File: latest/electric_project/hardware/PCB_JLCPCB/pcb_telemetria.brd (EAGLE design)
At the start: 106.8 x 121.5 mm, 39 parts

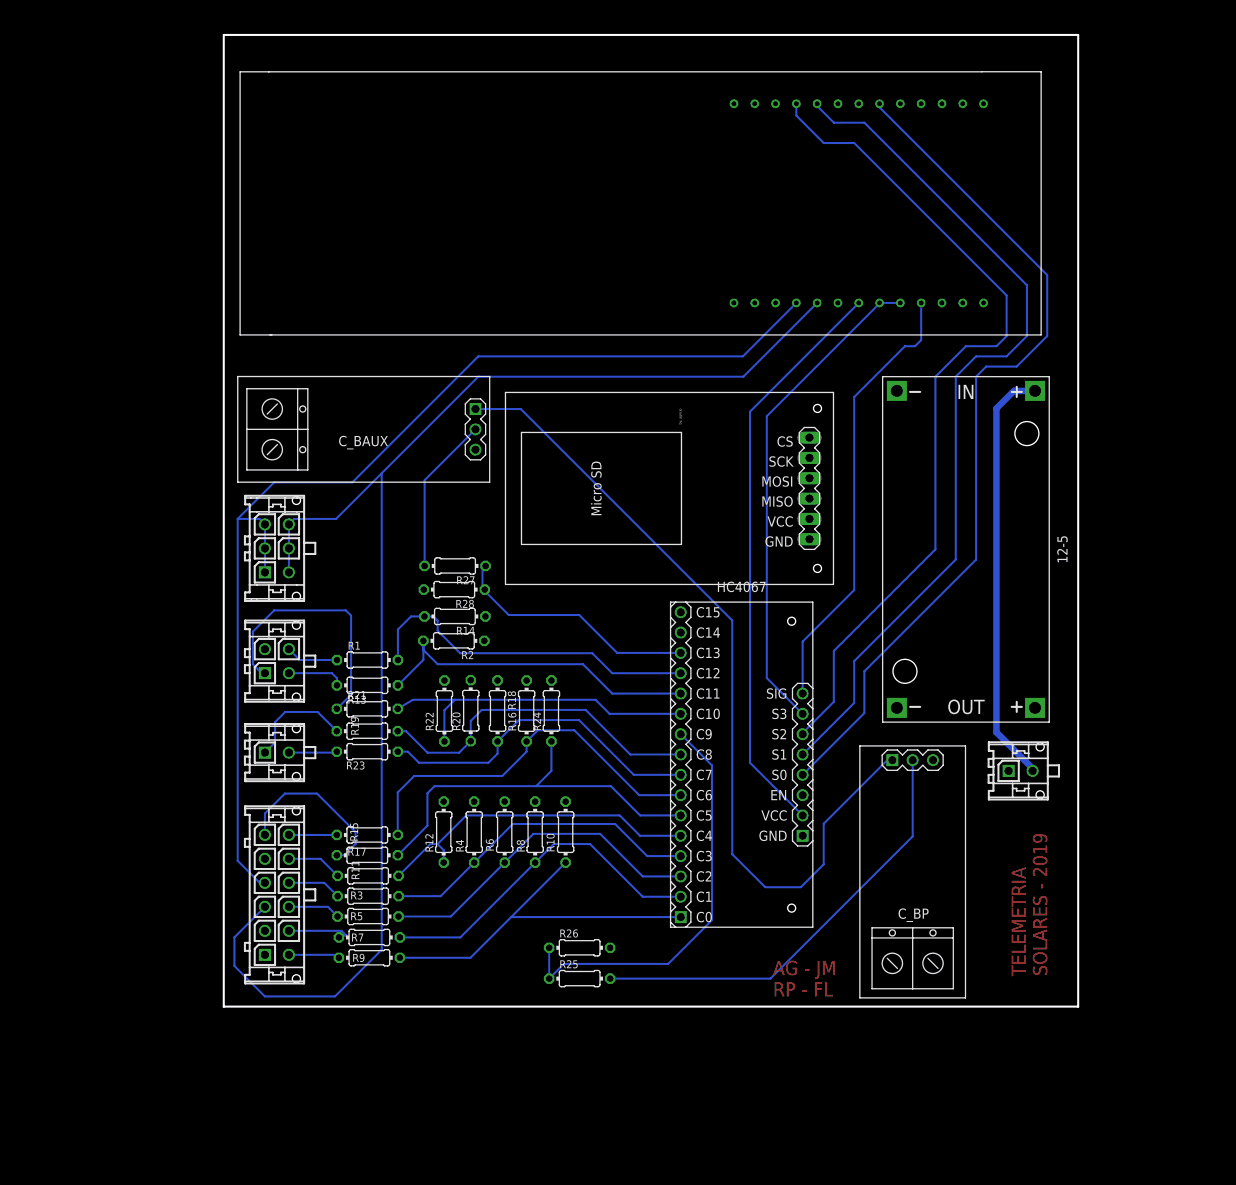
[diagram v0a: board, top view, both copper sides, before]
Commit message: adicao de conexao para pinos extras
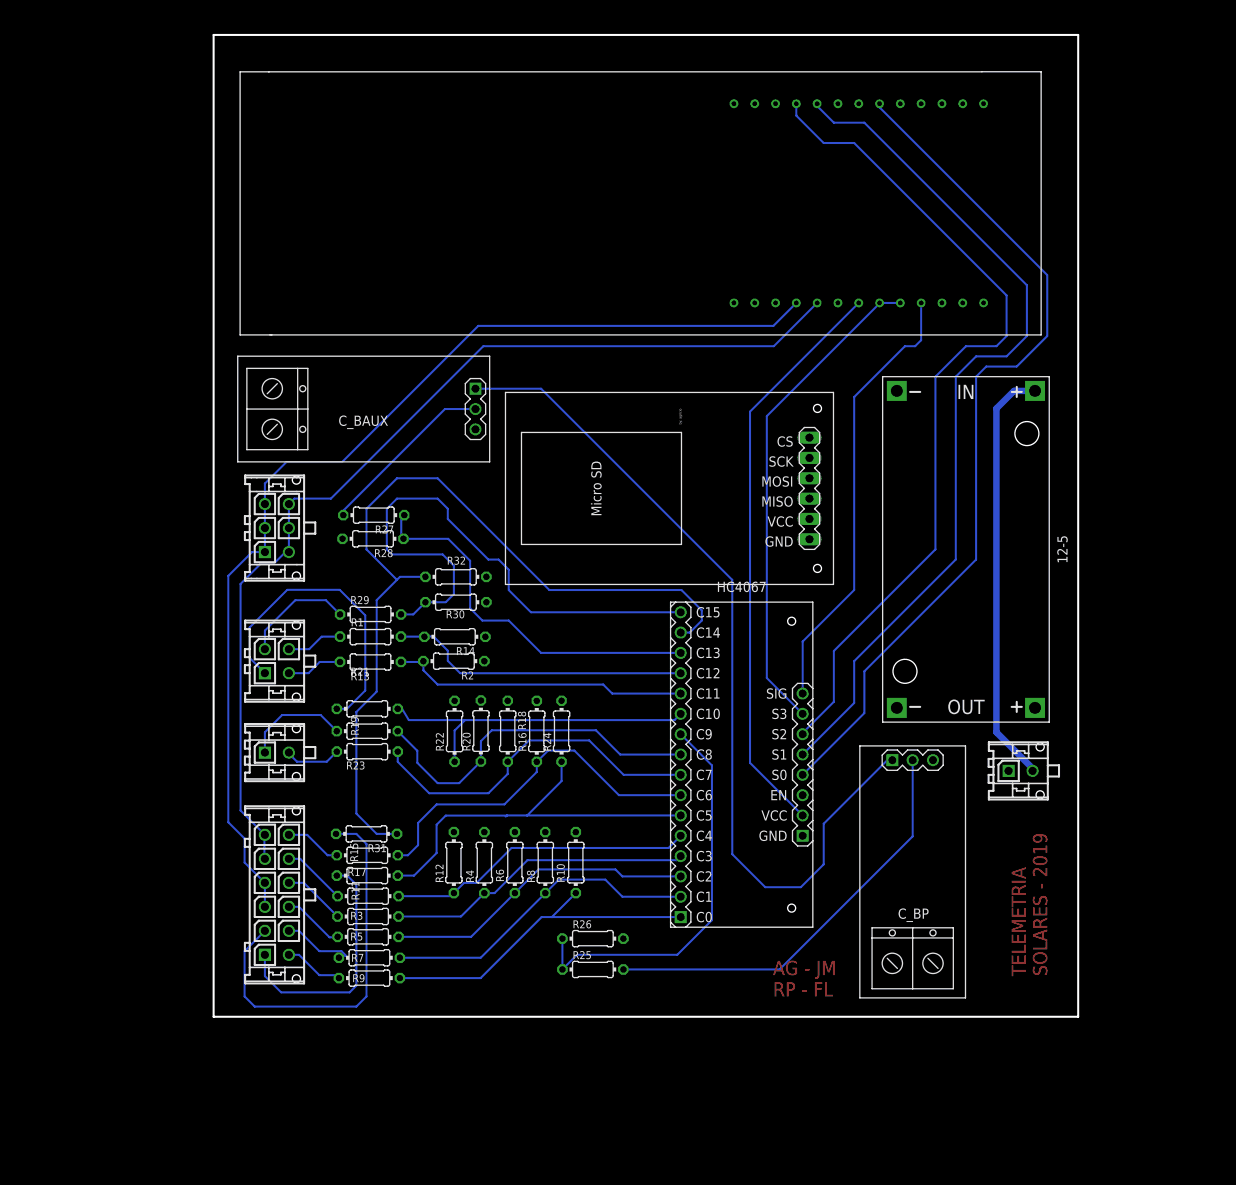
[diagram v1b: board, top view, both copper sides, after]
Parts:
- added R29, R31: 2.2k, rcl:0204/7
- added R30, R32: 3.9k, rcl:0204/7
- moved R27 12.0 mm to (22.5, 56.4)
- moved R28 12.0 mm to (22.4, 53.4)
- moved R10 4.02 mm to (47.8, 12.9)
- moved R4 4.02 mm to (36.3, 12.9)
- moved R8 4.02 mm to (43.9, 12.9)
- moved R12 4.02 mm to (32.5, 12.9)
- moved R6 4.02 mm to (40.1, 12.9)
- moved R1 2.95 mm to (22.1, 41.2)
- moved R13 2.95 mm to (22.1, 38.0)
- moved R22 2.84 mm to (32.6, 29.3)
- moved R16 2.84 mm to (42.9, 29.3)
- moved R18 2.84 mm to (39.2, 29.3)
- moved R20 2.84 mm to (35.9, 29.4)
- moved R24 2.84 mm to (46.0, 29.3)
- moved R11 2.54 mm to (21.8, 8.72)
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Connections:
- removed net N$5: X1.P$2
- removed net N$6: X1.P$1
- removed net N$8: X1.P$5
- new net EXTRA1: R29.1, X3.P$2
- new net EXTRA2: R31.2, X1.P$2
- net 21: now also X1.P$3
- net 22: now also X1.P$5, X1.P$6; no longer X1.P$3
- net BE_IN: now also X1.P$1; no longer X1.P$6
- net C14: now also R31.1, R32.2
- net C15: now also R29.2, R30.1
- net GND: now also R30.2, R32.1
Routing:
- net C14: track 0.00 -> 106.5 mm
- net C15: track 0.00 -> 70.9 mm
- net EXTRA2: track 0.00 -> 48.9 mm
- net 22: track 174.4 -> 126.0 mm
- net C13: track 31.1 -> 47.3 mm
- net EXTRA1: track 0.00 -> 14.0 mm
- net BE_IN: track 21.4 -> 30.8 mm
- net BAT_AUX: track 32.1 -> 38.1 mm
- net C12: track 43.5 -> 37.6 mm
- net C11: track 42.4 -> 37.4 mm
- net 21: track 138.0 -> 133.4 mm
- net C0: track 46.8 -> 42.5 mm
- net VCC: track 103.5 -> 107.6 mm
- net C4: track 42.1 -> 38.4 mm
- net C1: track 42.7 -> 40.0 mm
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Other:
- board size 106.8 x 121.5 mm -> 108.1 x 122.7 mm

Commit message: adding connector to sd card and capacitors
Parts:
- added C1, C2: 0.1uF, rcl:E5-5
- added C3: (no value), rcl:E5-5
- added X6: (no value), con-molex-micro-fit-3_0:43045-0412
- moved U$2 117.0 mm to (-10.2, -18.4), turned to 0 degrees
- moved X4 3.72 mm to (102.4, 20.7)
- moved C_BP 1.42 mm to (91.1, 12.4)
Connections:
- new net N$3: U$2.3, X6.P$4
- new net N$4: U$2.4, X6.P$3
- new net N$6: U$2.6, X6.P$1
- new net N$7: U$2.5, X6.P$2
- net GND: now also C1.-, C2.-, C3.-
- net VCC: now also C1.+, C3.+
- net VI: now also C2.+
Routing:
- net VCC: track 107.6 -> 143.0 mm
- net VI: track 52.9 -> 63.7 mm
- net N$1: track 52.6 -> 57.1 mm
- net 4: track 55.7 -> 55.0 mm

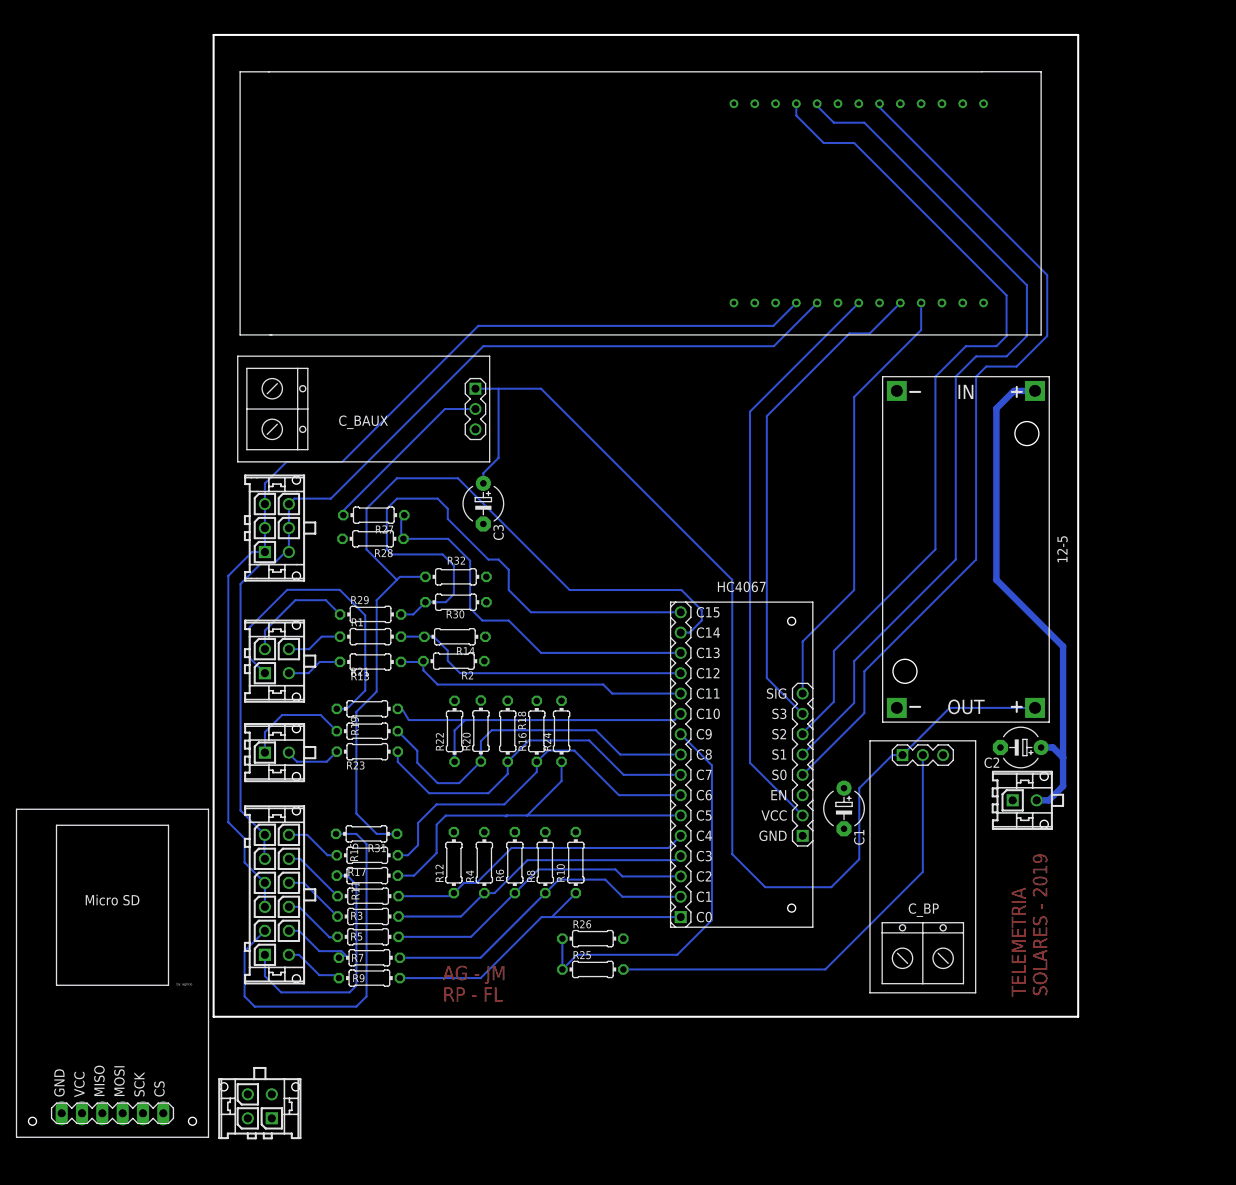
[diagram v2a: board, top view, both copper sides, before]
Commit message: adding connector to sdcard and ground plane
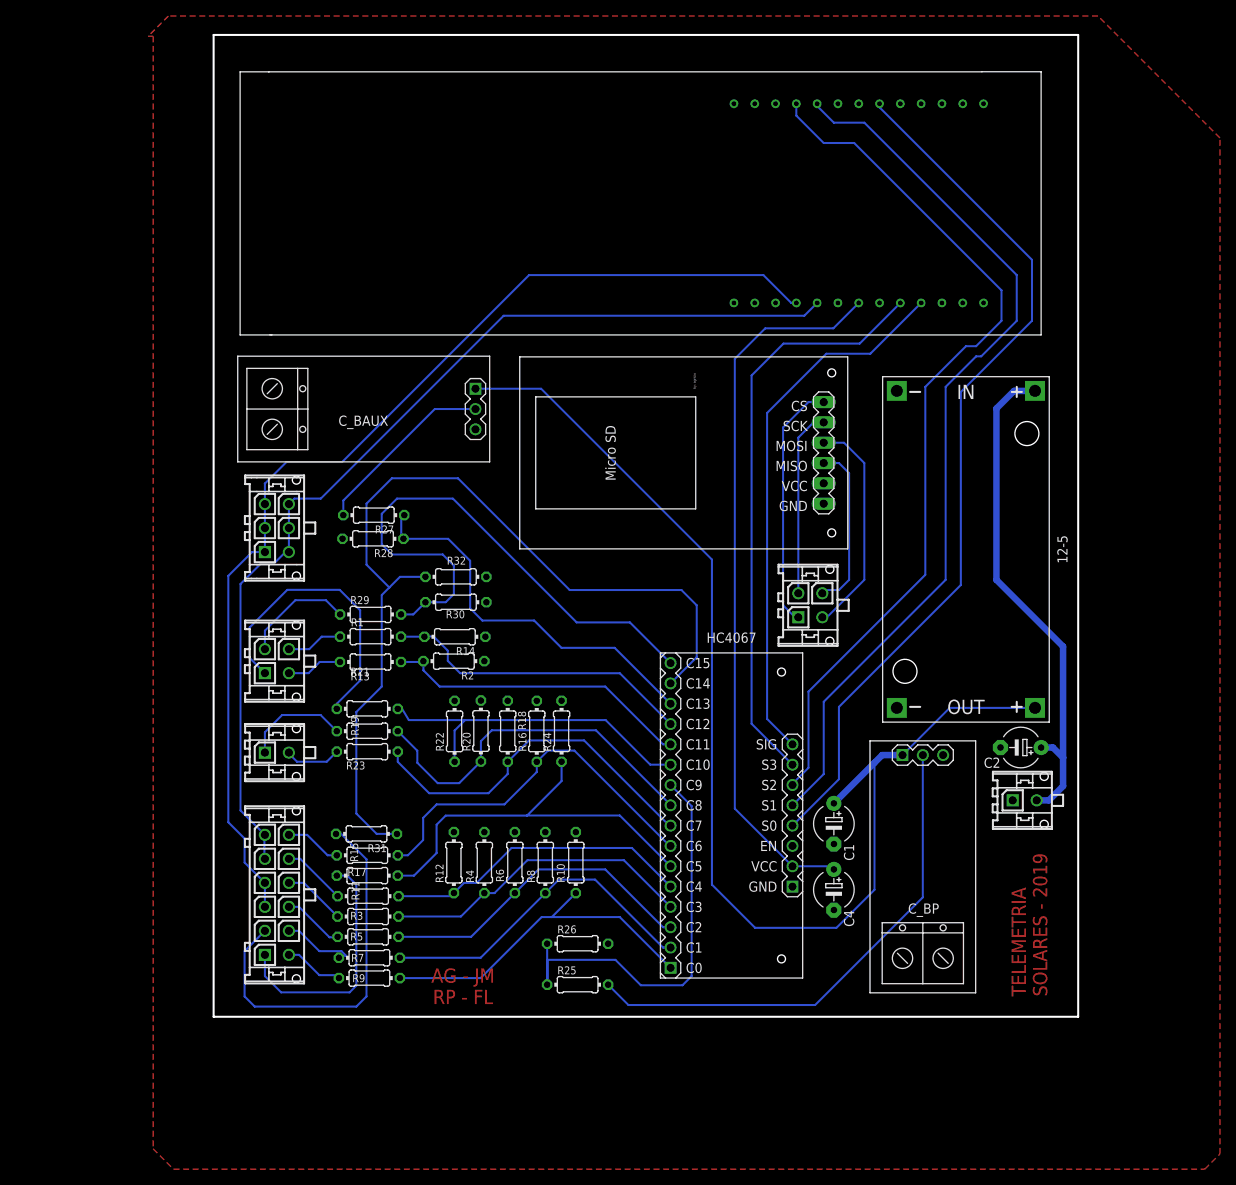
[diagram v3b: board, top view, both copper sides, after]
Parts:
- removed C3: (no value), rcl:E5-5
- added C4: (no value), rcl:E5-5
- moved U$2 121.3 mm to (78.7, 64.1), turned to 90 degrees
- moved X6 93.0 mm to (75.6, 45.1), turned to 270 degrees
- moved HC4067 6.48 mm to (67.2, 18.8)
- moved R25 2.69 mm to (48.0, -2.34)
- moved C1 2.29 mm to (80.0, 17.8)
- moved R26 2.01 mm to (48.0, 2.78)
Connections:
- net 3V3: now also C4.+
- net GND: now also C4.-; no longer C3.-
- net VCC: no longer C3.+
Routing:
- net N$6: track 0.00 -> 31.1 mm
- net N$4: track 0.00 -> 27.9 mm
- net N$7: track 0.00 -> 23.4 mm
- net N$3: track 0.00 -> 21.1 mm
- net 3V3: track 72.4 -> 90.1 mm
- net 4: track 55.0 -> 67.7 mm
- net 0: track 61.6 -> 73.1 mm
- net N$1: track 57.1 -> 63.7 mm
- net C14: track 106.5 -> 113.1 mm
- net VCC: track 143.0 -> 149.5 mm
- net 13: track 104.7 -> 109.6 mm
- net 14: track 108.3 -> 112.2 mm
- net 32: track 107.5 -> 110.5 mm
- net C9: track 50.0 -> 53.0 mm
- net 21: track 133.4 -> 136.3 mm
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- added copper zone on layer 1, net GND

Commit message: up
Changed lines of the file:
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@@
 <?xml version="1.0" encoding="utf-8"?>
 <!DOCTYPE eagle SYSTEM "eagle.dtd">
-<eagle version="9.5.0">
+<eagle version="9.5.1">
 <drawing>
 <settings>
@@
 <wire x1="74.83855625" y1="22.621246875" x2="74.83855625" y2="22.76855625" width="0.254" layer="16"/>
 <wire x1="74.83855625" y1="22.76855625" x2="76.835" y2="24.765" width="0.254" layer="16"/>
-<wire x1="76.835" y1="24.765" x2="76.835" y2="34.29" width="0.254" layer="16"/>
-<wire x1="91.44" y1="48.895" x2="91.44" y2="72.39" width="0.254" layer="16"/>
+<wire x1="76.835" y1="24.765" x2="76.835" y2="33.655" width="0.254" layer="16"/>
+<wire x1="91.44" y1="48.26" x2="91.44" y2="72.39" width="0.254" layer="16"/>
 <wire x1="91.44" y1="72.39" x2="96.52" y2="77.47" width="0.254" layer="16"/>
 <wire x1="97.79" y1="77.47" x2="100.965" y2="80.645" width="0.254" layer="16"/>
@@
 <wire x1="78.74" y1="102.87" x2="75.31951875" y2="106.29048125" width="0.254" layer="16"/>
 <wire x1="75.31951875" y1="106.29048125" x2="75.31951875" y2="107.777559375" width="0.254" layer="16"/>
-<wire x1="76.835" y1="34.29" x2="91.44" y2="48.895" width="0.254" layer="16"/>
+<wire x1="76.835" y1="33.655" x2="91.44" y2="48.26" width="0.254" layer="16"/>
 <wire x1="96.52" y1="77.47" x2="97.79" y2="77.47" width="0.254" layer="16"/>
 <wire x1="100.965" y1="84.455" x2="82.55" y2="102.87" width="0.254" layer="16"/>
@@
 <vertex x="-5.715" y="116.205"/>
 </polygon>
+<wire x1="80.51951875" y1="82.877559375" x2="70.11951875" y2="107.777559375" width="0" layer="19" extent="1-1"/>
+<wire x1="87.884" y1="71.882" x2="80.51951875" y2="82.877559375" width="0" layer="19" extent="1-1"/>
+<wire x1="87.884" y1="32.258" x2="87.884" y2="71.882" width="0" layer="19" extent="1-1"/>
+<wire x1="93.670121875" y1="26.360109375" x2="87.884" y2="32.258" width="0" layer="19" extent="1-1"/>
+<wire x1="100.838" y1="27.305" x2="93.670121875" y2="26.360109375" width="0" layer="19" extent="1-1"/>
+<wire x1="102.362" y1="20.701" x2="100.838" y2="27.305" width="0" layer="19" extent="1-1"/>
+<wire x1="80.01" y1="15.24" x2="93.670121875" y2="26.360109375" width="0" layer="19" extent="1-1"/>
+<wire x1="74.83855625" y1="15.001246875" x2="80.01" y2="15.24" width="0" layer="19" extent="1-1"/>
+<wire x1="74.83855625" y1="9.921246875" x2="74.83855625" y2="15.001246875" width="0" layer="19" extent="1-1"/>
+<wire x1="80.01" y1="6.985" x2="74.83855625" y2="9.921246875" width="0" layer="19" extent="1-1"/>
+<wire x1="51.7906" y1="2.778759375" x2="74.83855625" y2="9.921246875" width="0" layer="19" extent="1-1"/>
+<wire x1="47.752" y1="16.728446875" x2="51.7906" y2="2.778759375" width="0" layer="19" extent="1-1"/>
+<wire x1="43.942" y1="16.728446875" x2="47.752" y2="16.728446875" width="0" layer="19" extent="1-1"/>
+<wire x1="40.132" y1="16.728446875" x2="43.942" y2="16.728446875" width="0" layer="19" extent="1-1"/>
+<wire x1="36.322" y1="16.728446875" x2="40.132" y2="16.728446875" width="0" layer="19" extent="1-1"/>
+<wire x1="32.512" y1="16.728446875" x2="36.322" y2="16.728446875" width="0" layer="19" extent="1-1"/>
+<wire x1="32.5983625" y1="33.13684375" x2="32.512" y2="16.728446875" width="0" layer="19" extent="1-1"/>
+<wire x1="35.89020625" y1="33.177484375" x2="32.5983625" y2="33.13684375" width="0" layer="19" extent="1-1"/>
+<wire x1="39.243" y1="33.147" x2="35.89020625" y2="33.177484375" width="0" layer="19" extent="1-1"/>
+<wire x1="42.87520625" y1="33.13684375" x2="39.243" y2="33.147" width="0" layer="19" extent="1-1"/>
+<wire x1="36.322" y1="38.1" x2="35.89020625" y2="33.177484375" width="0" layer="19" extent="1-1"/>
+<wire x1="36.449" y1="41.148" x2="36.322" y2="38.1" width="0" layer="19" extent="1-1"/>
+<wire x1="36.576" y1="45.466" x2="36.449" y2="41.148" width="0" layer="19" extent="1-1"/>
+<wire x1="36.576" y1="48.641" x2="36.576" y2="45.466" width="0" layer="19" extent="1-1"/>
+<wire x1="35.209478125" y1="67.076315625" x2="36.576" y2="48.641" width="0" layer="19" extent="1-1"/>
+<wire x1="18.590259375" y1="53.393340625" x2="36.576" y2="48.641" width="0" layer="19" extent="1-1"/>
 </signal>
 <signal name="22">
 <contactref element="U$1" pad="22"/>
-<wire x1="15.875" y1="58.42" x2="38.735" y2="81.28" width="0.254" layer="16"/>
+<wire x1="17.145" y1="58.42" x2="40.005" y2="81.28" width="0.254" layer="16"/>
 <wire x1="76.321946875" y1="81.2799875" x2="77.91951875" y2="82.877559375" width="0.254" layer="16"/>
-<wire x1="76.321946875" y1="81.2799875" x2="38.735" y2="81.28" width="0.254" layer="16"/>
+<wire x1="76.321946875" y1="81.2799875" x2="40.005" y2="81.28" width="0.254" layer="16"/>
 <contactref element="X5" pad="P$5"/>
 <contactref element="X5" pad="P$6"/>
 <contactref element="X5" pad="P$4"/>
 <wire x1="11.89" y1="51.737" x2="11.89" y2="52.07" width="0.254" layer="16"/>
-<wire x1="11.89" y1="52.07" x2="11.89" y2="54.61" width="0.254" layer="16"/>
+<wire x1="11.89" y1="52.07" x2="11.89" y2="54.737" width="0.254" layer="16"/>
 <wire x1="11.89" y1="54.737" x2="11.89" y2="57.737" width="0.254" layer="16"/>
 <wire x1="11.89" y1="57.737" x2="12.573" y2="58.42" width="0.254" layer="16"/>
-<wire x1="12.573" y1="58.42" x2="15.875" y2="58.42" width="0.254" layer="16"/>
+<wire x1="12.573" y1="58.42" x2="17.145" y2="58.42" width="0.254" layer="16"/>
 <contactref element="X1" pad="P$6"/>
 <wire x1="8.89" y1="16.39" x2="8.83" y2="16.45" width="0.254" layer="16"/>
@@
 <wire x1="8.89" y1="13.39" x2="8.83" y2="13.45" width="0.254" layer="16"/>
 <wire x1="8.83" y1="13.45" x2="8.83" y2="16.45" width="0.254" layer="16"/>
-<wire x1="11.89" y1="54.737" x2="11.89" y2="54.61" width="0.254" layer="16"/>
 </signal>
 <signal name="21">
 <contactref element="U$1" pad="21"/>
-<wire x1="71.202103125" y1="86.359975" x2="41.91" y2="86.36" width="0.254" layer="16"/>
+<wire x1="71.202103125" y1="86.359975" x2="42.545" y2="86.36" width="0.254" layer="16"/>
 <wire x1="8.8782" y1="60.2888" x2="11.5814" y2="62.992" width="0.254" layer="16"/>
-<wire x1="11.5814" y1="62.992" x2="18.542" y2="62.992" width="0.254" layer="16"/>
-<wire x1="18.542" y1="62.992" x2="41.91" y2="86.36" width="0.254" layer="16"/>
+<wire x1="11.5814" y1="62.992" x2="19.177" y2="62.992" width="0.254" layer="16"/>
+<wire x1="19.177" y1="62.992" x2="42.545" y2="86.36" width="0.254" layer="16"/>
 <contactref element="X5" pad="P$2"/>
 <contactref element="X5" pad="P$1"/>
